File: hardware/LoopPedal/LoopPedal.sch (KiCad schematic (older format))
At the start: 17 parts, among them J1 Input, J2 Output, J3 Footpedal, SW1 Primary Button, SW2 Secondary Button, U1 6N138, U2 Teensy4.1

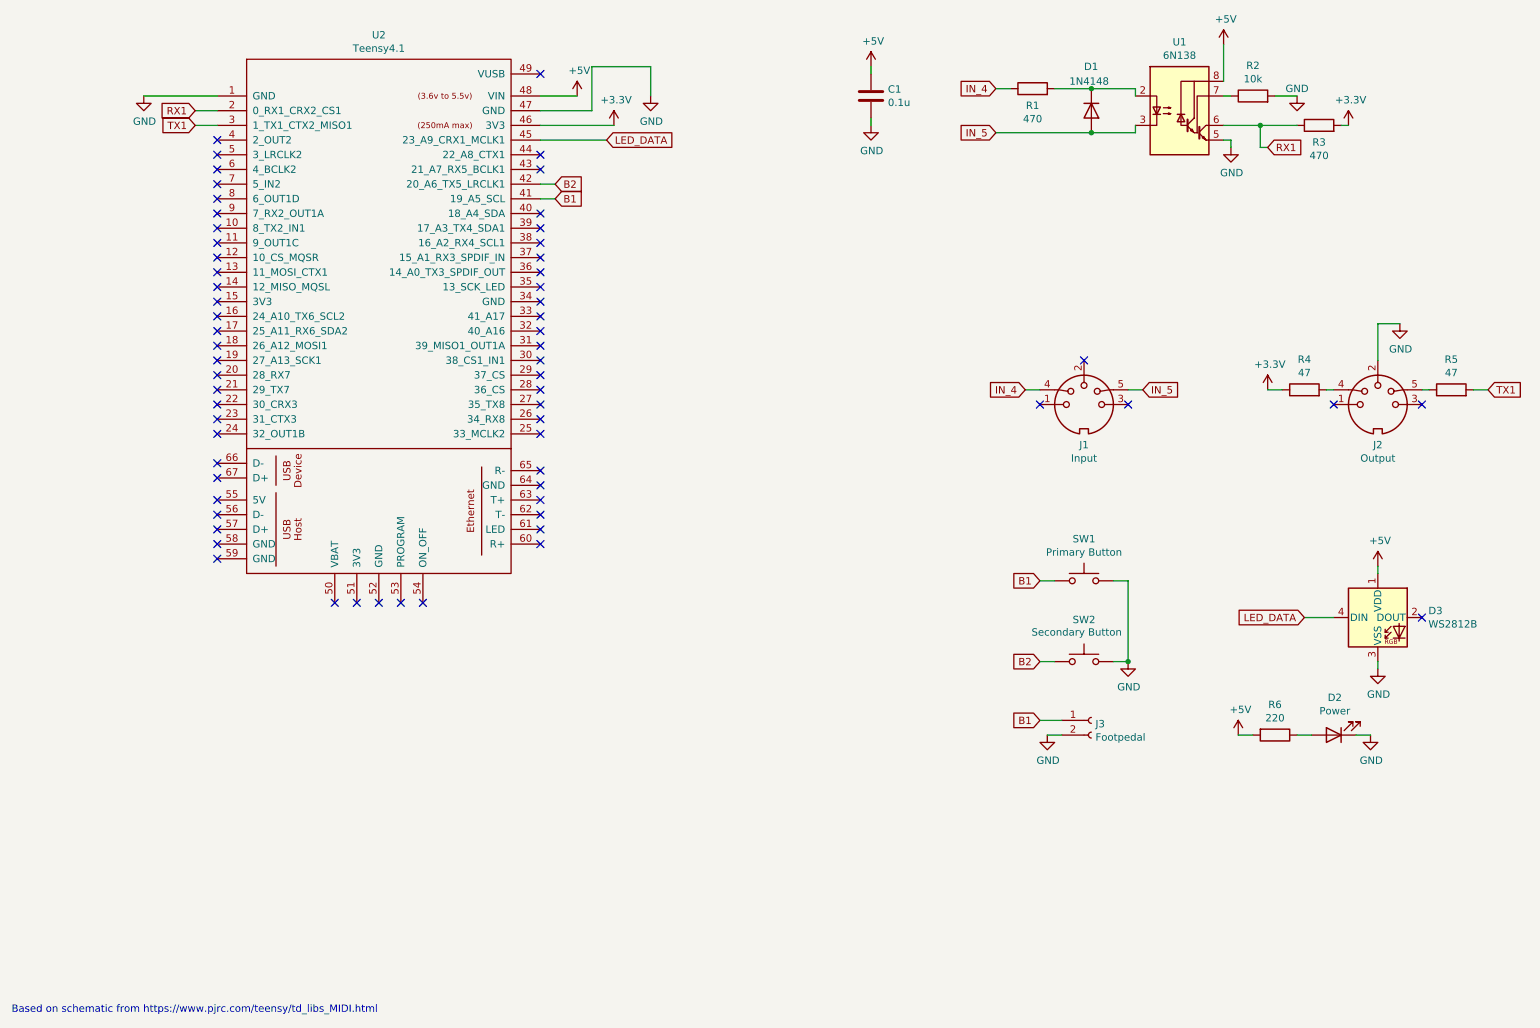
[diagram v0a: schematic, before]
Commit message: Update pin mapping to reflect proto-board layout
MIDI was moved from Serial1 to Serial 7.
Button 2 was moved from pin 20 to pin 18.
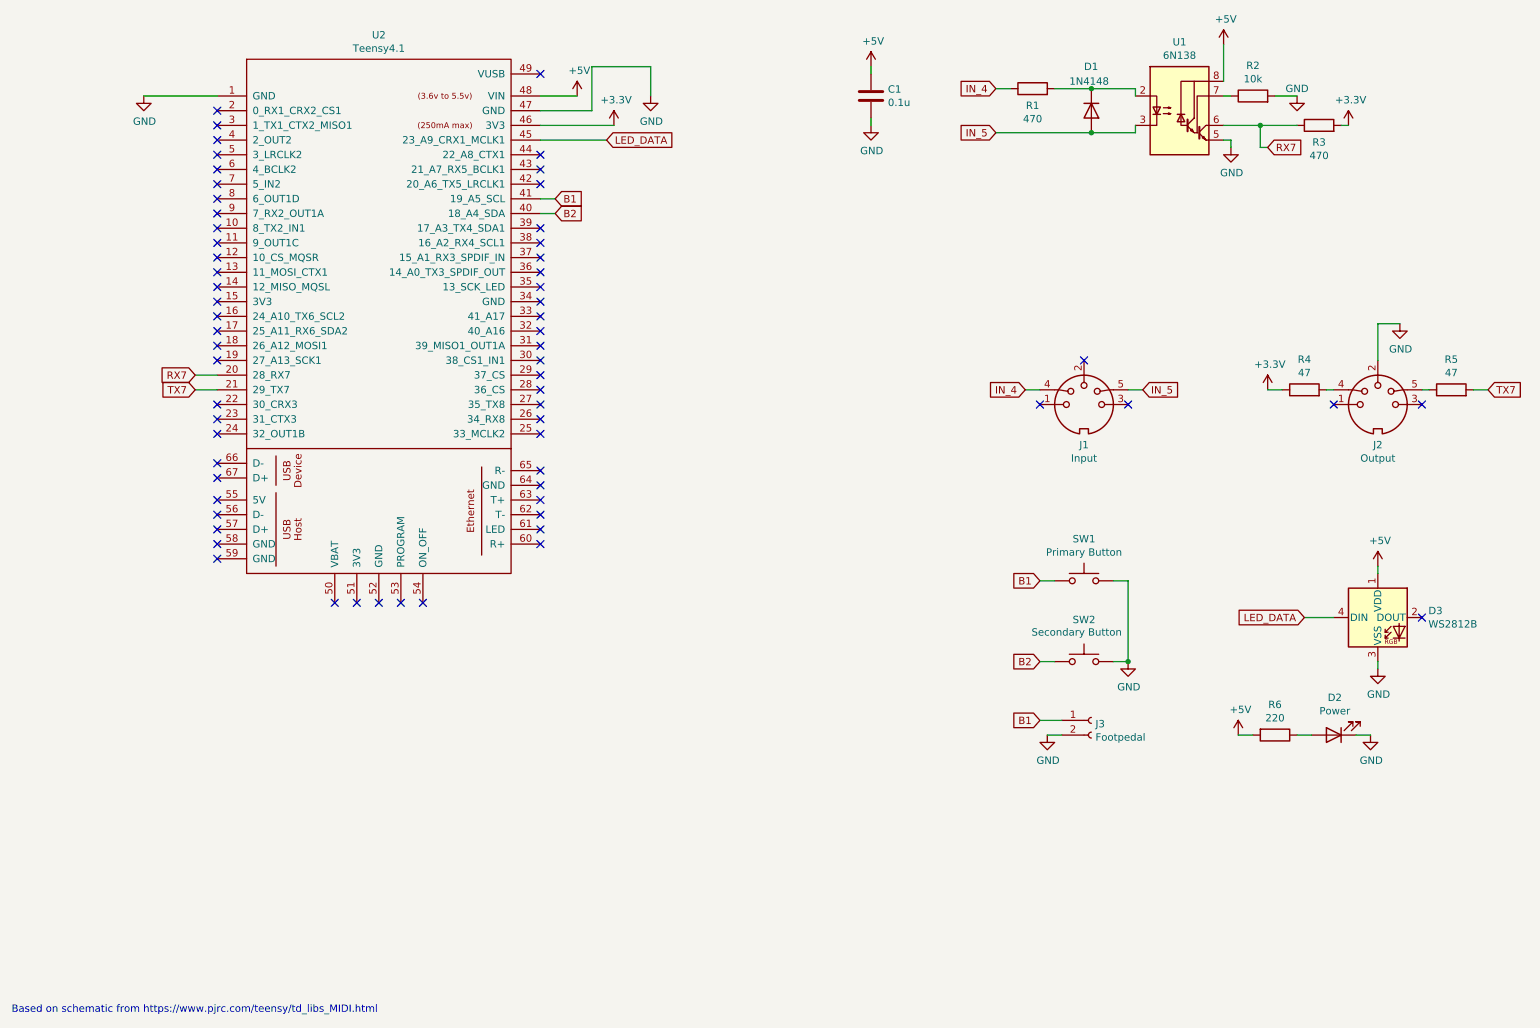
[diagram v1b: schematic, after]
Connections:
- net B2: now also U2.40 (18_A4_SDA); no longer U2.42 (20_A6_TX5_LRCLK1)
- net RX7: now reaches U2.20 (28_RX7)
- net RX7: now also R3.1, U1.6 (VO2)
- net TX7: now reaches U2.21 (29_TX7)
- net TX7: now also R5.2
- removed net RX1: R3.1, U1.6 (VO2), U2.2 (0_RX1_CRX2_CS1)
- net TX1: no longer names the net of U2.3 (1_TX1_CTX2_MISO1)
- net TX1: no longer R5.2
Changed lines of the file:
@@
 $EndComp
 Text GLabel 9050 1850 2    50   Input ~ 0
-RX1
-Text GLabel 1750 1600 0    50   Input ~ 0
-RX1
-Wire Wire Line
-	1750 1600 1900 1600
-Text GLabel 1750 1700 0    50   Input ~ 0
-TX1
-Wire Wire Line
-	1750 1700 1900 1700
+RX7
+Text GLabel 1750 3400 0    50   Input ~ 0
+RX7
+Wire Wire Line
+	1750 3400 1900 3400
+Text GLabel 1750 3500 0    50   Input ~ 0
+TX7
+Wire Wire Line
+	1750 3500 1900 3500
 Wire Wire Line
 	6350 1300 6350 1350
@@
 $EndComp
 Text GLabel 10550 3500 2    50   Input ~ 0
-TX1
+TX7
 Wire Wire Line
 	9050 3500 9150 3500
@@
 NoConn ~ 4100 2500
 NoConn ~ 4100 2400
-NoConn ~ 4100 2300
 NoConn ~ 4100 2000
 NoConn ~ 4100 1900
@@
 NoConn ~ 1900 3700
 NoConn ~ 1900 3600
-NoConn ~ 1900 3500
-NoConn ~ 1900 3400
 NoConn ~ 1900 3300
 NoConn ~ 1900 3200
@@
 Text GLabel 4200 2200 2    50   Input ~ 0
 B1
-Text GLabel 4200 2100 2    50   Input ~ 0
+Text GLabel 4200 2300 2    50   Input ~ 0
 B2
 Wire Wire Line
-	4200 2100 4100 2100
+	4200 2300 4100 2300
 Wire Wire Line
 	4200 2200 4100 2200
@@
 Wire Wire Line
 	9000 1700 9250 1700
+NoConn ~ 1900 1600
+NoConn ~ 1900 1700
+NoConn ~ 4100 2100
 $EndSCHEMATC

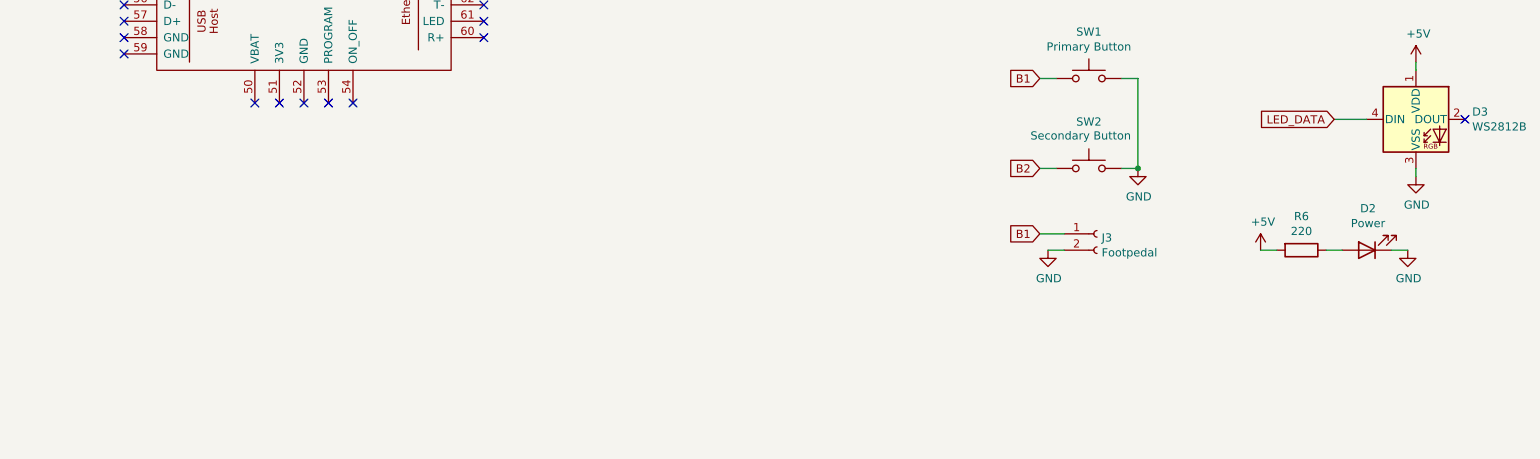
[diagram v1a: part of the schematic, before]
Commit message: Update schematic and BOM. Add Phase III deliverables
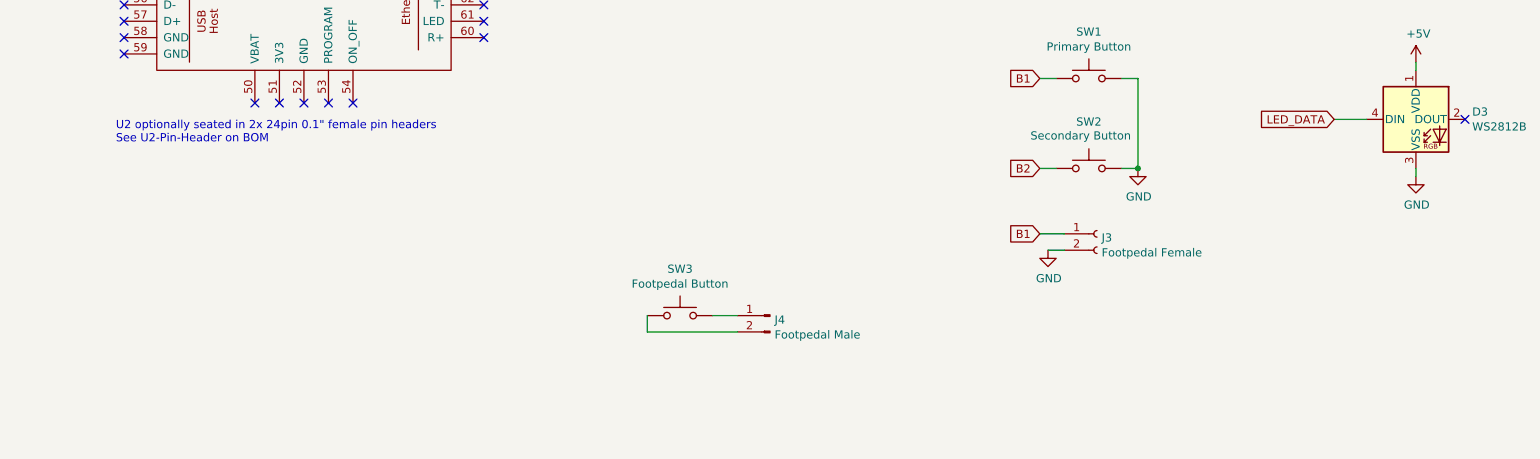
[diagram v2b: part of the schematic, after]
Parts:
- removed D2: Power, symbol Device:LED
- removed R6: 220, symbol Device:R
- added J4: Footpedal Male, symbol Connector:Conn_01x02_Male
- added SW3: Footpedal Button, symbol Switch:SW_Push
- J3: value Footpedal -> Footpedal Female
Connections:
- new net: J4.2 (Pin_2), SW3.1
- new net: J4.1 (Pin_1), SW3.2
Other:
- note added: "U2 optionally seated in 2x 24pin 0.1" female pin headers\nSee U2-Pin-Header on BOM"
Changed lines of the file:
@@
 P 7850 5750
 F 0 "J3" H 7878 5726 50  0000 L CNN
-F 1 "Footpedal" H 7878 5635 50  0000 L CNN
+F 1 "Footpedal Female" H 7878 5635 50  0000 L CNN
 F 2 "" H 7850 5750 50  0001 C CNN
 F 3 "~" H 7850 5750 50  0001 C CNN
@@
 Based on schematic from https://www.pjrc.com/teensy/td_libs_MIDI.html
 $Comp
-L Device:LED D2
-U 1 1 613F1F7F
-P 9500 5850
-F 0 "D2" H 9493 5595 50  0000 C CNN
-F 1 "Power" H 9493 5686 50  0000 C CNN
-F 2 "" H 9500 5850 50  0001 C CNN
-F 3 "~" H 9500 5850 50  0001 C CNN
-	1    9500 5850
-	-1   0    0    1
-$EndComp
-$Comp
-L Device:R R6
-U 1 1 613F25D0
-P 9100 5850
-F 0 "R6" V 8893 5850 50  0000 C CNN
-F 1 "220" V 8984 5850 50  0000 C CNN
-F 2 "" V 9030 5850 50  0001 C CNN
-F 3 "~" H 9100 5850 50  0001 C CNN
-	1    9100 5850
-	0    1    1    0
-$EndComp
-Wire Wire Line
-	9250 5850 9350 5850
-$Comp
-L power:GND #PWR06
-U 1 1 613F4184
-P 9750 5850
-F 0 "#PWR06" H 9750 5600 50  0001 C CNN
-F 1 "GND" H 9755 5677 50  0000 C CNN
-F 2 "" H 9750 5850 50  0001 C CNN
-F 3 "" H 9750 5850 50  0001 C CNN
-	1    9750 5850
-	1    0    0    -1
-$EndComp
-Wire Wire Line
-	9650 5850 9750 5850
-$Comp
-L power:+5V #PWR05
-U 1 1 613F66F8
-P 8850 5850
-F 0 "#PWR05" H 8850 5700 50  0001 C CNN
-F 1 "+5V" H 8865 6023 50  0000 C CNN
-F 2 "" H 8850 5850 50  0001 C CNN
-F 3 "" H 8850 5850 50  0001 C CNN
-	1    8850 5850
-	1    0    0    -1
-$EndComp
-Wire Wire Line
-	8850 5850 8950 5850
-$Comp
 L LED:WS2812B D3
 U 1 1 61405613
@@
 NoConn ~ 1900 1700
 NoConn ~ 4100 2100
+Text Notes 1850 5200 0    50   ~ 0
+U2 optionally seated in 2x 24pin 0.1" female pin headers\nSee U2-Pin-Header on BOM
+$Comp
+L Switch:SW_Push SW3
+U 1 1 614D41FB
+P 5300 6250
+F 0 "SW3" H 5300 6535 50  0000 C CNN
+F 1 "Footpedal Button" H 5300 6444 50  0000 C CNN
+F 2 "" H 5300 6450 50  0001 C CNN
+F 3 "~" H 5300 6450 50  0001 C CNN
+	1    5300 6250
+	1    0    0    -1
+$EndComp
+$Comp
+L Connector:Conn_01x02_Male J4
+U 1 1 614DBEF8
+P 5850 6250
+F 0 "J4" H 5822 6224 50  0000 R CNN
+F 1 "Footpedal Male" H 5822 6133 50  0000 R CNN
+F 2 "" H 5850 6250 50  0001 C CNN
+F 3 "~" H 5850 6250 50  0001 C CNN
+	1    5850 6250
+	-1   0    0    -1
+$EndComp
+Wire Wire Line
+	5500 6250 5650 6250
+Wire Wire Line
+	5650 6350 5100 6350
+Wire Wire Line
+	5100 6350 5100 6250
 $EndSCHEMATC
